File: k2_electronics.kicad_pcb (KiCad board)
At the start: 2 copper layers, 152.1 x 87.5 mm, 62 parts, among them J1 Conn_02x03_Odd_Even, Q1 Q_NMOS_GSD, SW1 SW_SPST, SW10 SW_SPST, SW11 SW_SPST, SW12 SW_SPST, SW13 SW_SPST, SW14 SW_SPST, SW15 SW_SPST, SW16 SW_SPST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

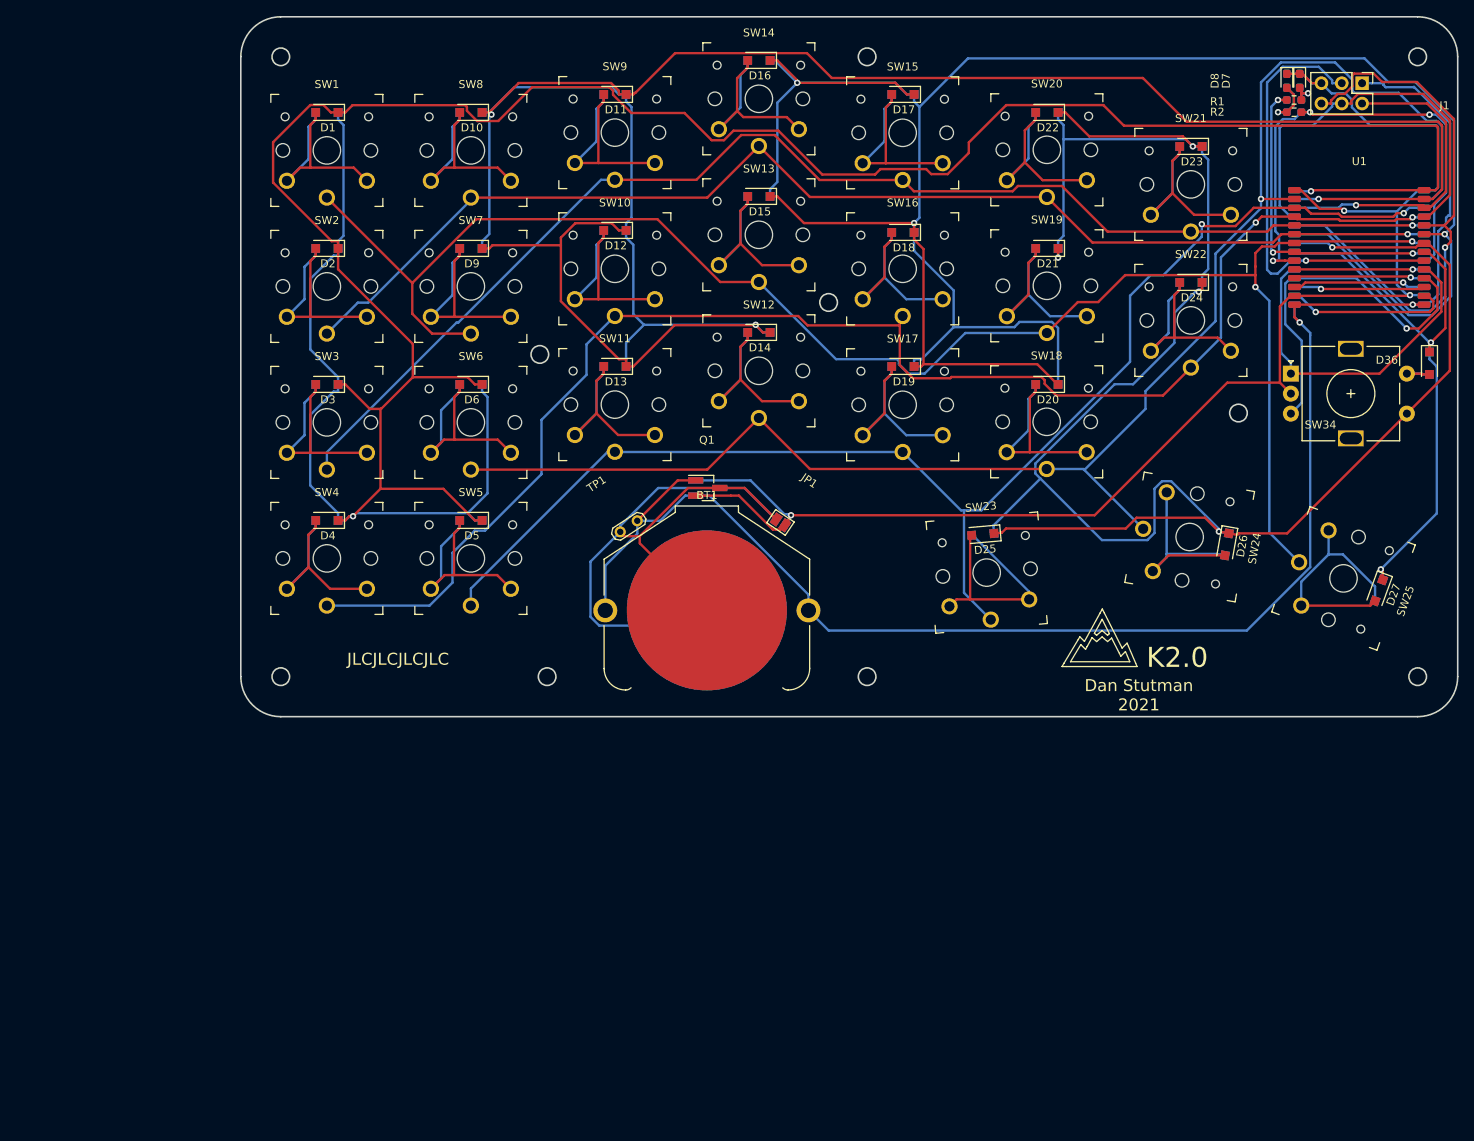
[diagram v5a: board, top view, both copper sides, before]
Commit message: Switch to NPTH holes
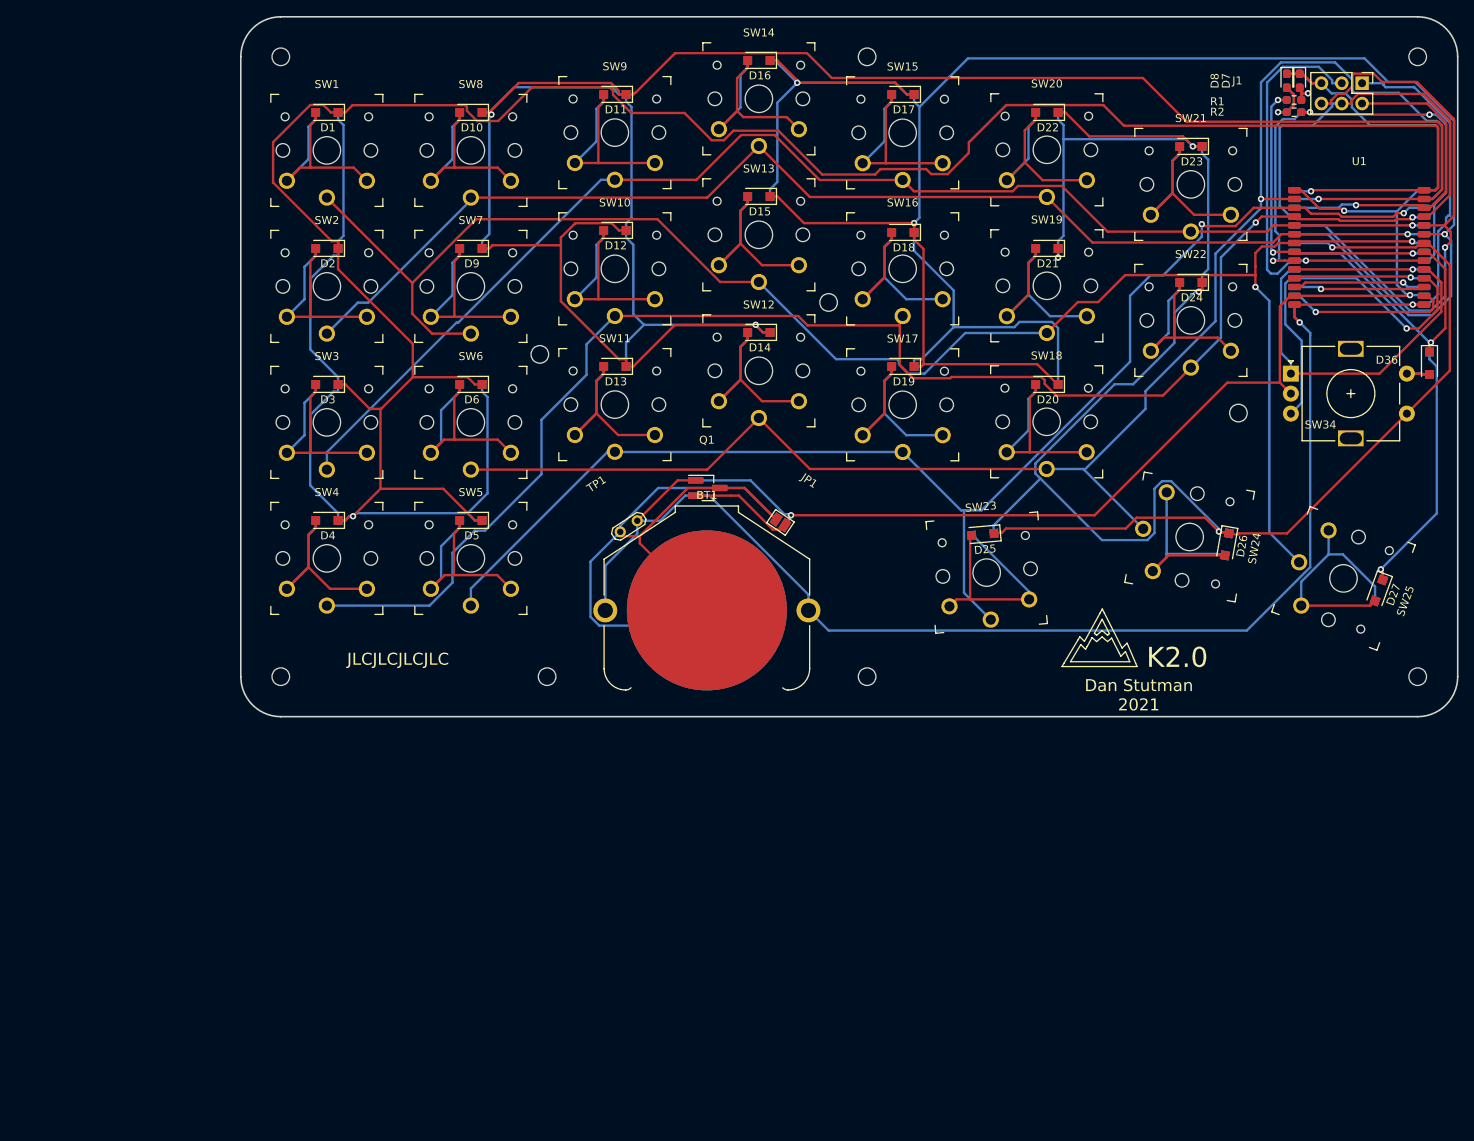
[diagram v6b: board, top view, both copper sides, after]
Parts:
- added REF**: M2 Hole, k2:M2_Hole, F.Cu at (158.5, 132.8)
- added REF**: M2 Hole, k2:M2_Hole, F.Cu at (85.2, 132.8)
- added REF**: M2 Hole, k2:M2_Hole, F.Cu at (158.5, 55.3)
- added REF**: M2 Hole, k2:M2_Hole, F.Cu at (227.4, 55.3)
- added REF**: M2 Hole, k2:M2_Hole, F.Cu at (204.9, 99.8)
- added REF**: M2 Hole, k2:M2_Hole, F.Cu at (227.4, 132.8)
- added REF**: M2 Hole, k2:M2_Hole, F.Cu at (153.7, 86.0)
- added REF**: M2 Hole, k2:M2_Hole, F.Cu at (85.2, 55.3)
- added REF**: M2 Hole, k2:M2_Hole, F.Cu at (117.6, 92.5)
- added REF**: M2 Hole, k2:M2_Hole, F.Cu at (118.5, 132.8)
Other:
- outline, holes or cut-outs redrawn

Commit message: PCB mount
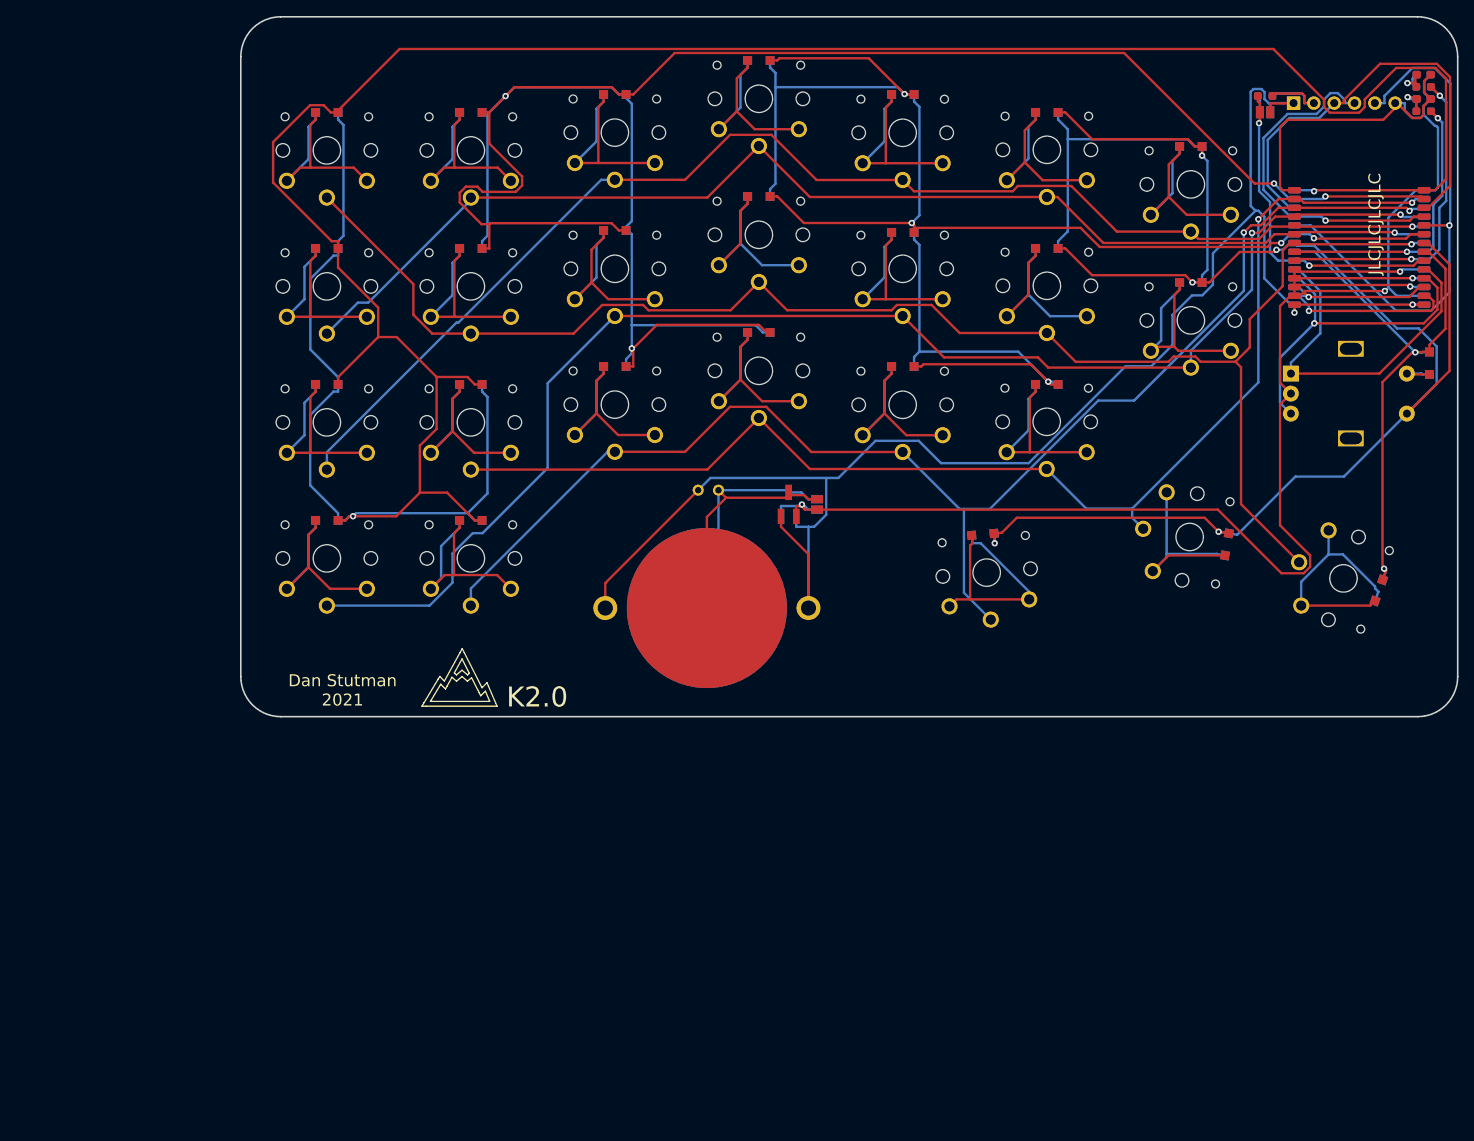
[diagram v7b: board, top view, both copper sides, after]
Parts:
- removed REF** (x10): M2 Hole, k2:M2_Hole
- added JP4: SolderJumper_2_Open, k2:SolderJumper-2_P1.3mm_Open_Pad1.0x1.5mm_reversible, F.Cu at (208.3, 62.2)
- added R3: R_Small_US, k2:R_0603_1608Metric_Pad0.98x0.95mm_HandSolder_reversible, F.Cu at (208.3, 60.2)
- J1: value Conn_02x03_Odd_Even -> Conn_01x06; footprint Connector_PinHeader_2.54mm:PinHeader_2x03_P2.54mm_Vertical -> k2:PinHeader_1x06_P2.54mm_Horizontal
- SW34: footprint Rotary_Encoder:RotaryEncoder_Alps_EC11E-Switch_Vertical_H20mm -> k2:RotaryEncoder_Alps_EC11E-Switch_Vertical_H20mm
- TP1: footprint TestPoint:TestPoint_2Pads_Pitch2.54mm_Drill0.8mm -> k2:TestPoint_2Pads_Pitch2.54mm_Drill0.8mm
- moved D8 17.1 mm to (228.1, 57.5), turned to 180 degrees
- moved R2 16.5 mm to (228.1, 59.1)
- moved R1 16.3 mm to (228.1, 62.1), turned to 0 degrees
- moved D7 15.7 mm to (228.1, 60.6), turned to 180 degrees
- moved Q1 10.3 mm to (148.7, 111.3), turned to 90 degrees
- moved J1 8.92 mm to (211.8, 61.1), turned to 90 degrees
- moved TP1 8.52 mm to (137.4, 109.5), turned to 0 degrees
- moved JP1 5.10 mm to (152.3, 111.3), turned to 270 degrees
- moved BT1 0.29 mm to (138.5, 124.2)
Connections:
- J1 pad 2: /SWCLK -> Net-(J1-Pad2)
- J1 pad 3: /~RESET -> /SWCLK
- J1 pad 5: GND -> /SWO
- J1 pad 6: /SWO -> GND
- U1 pad 10: Net-(U1-Pad10) -> GND
- U1 pad 11: Net-(U1-Pad11) -> GND
- U1 pad 12: Net-(U1-Pad12) -> GND
- U1 pad 16: Net-(U1-Pad16) -> GND
- U1 pad 17: Net-(U1-Pad17) -> GND
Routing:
- net GND: track 194.1 -> 297.8 mm, vias 3 -> 7
- net Net-(D15-Pad1): track 294.7 -> 215.0 mm, vias 3 -> 5
- net Net-(SW12-Pad1): track 192.7 -> 158.0 mm, vias 1 -> 2
- net Net-(BT1-Pad2): track 88.4 -> 56.5 mm
- net Net-(D21-Pad1): track 257.9 -> 229.6 mm
- net Net-(U1-Pad16): track 20.7 -> 0.00 mm, vias 1 -> 0
- net Net-(R2-Pad1): track 62.6 -> 41.9 mm, vias 3 -> 2
- net Net-(SW1-Pad1): track 212.0 -> 194.2 mm, vias 2 -> 1
- net Net-(U1-Pad12): track 16.7 -> 0.00 mm, vias 1 -> 0
- net Net-(D10-Pad1): track 305.3 -> 288.8 mm, vias 3 -> 4
- net Net-(U1-Pad17): track 16.4 -> 0.00 mm, vias 1 -> 0
- net Net-(U1-Pad11): track 16.4 -> 0.00 mm, vias 1 -> 0
- net Net-(U1-Pad10): track 16.2 -> 0.00 mm, vias 1 -> 0
- net /SWCLK: track 40.3 -> 55.8 mm, vias 1 -> 0
- net Net-(J1-Pad2): track 0.00 -> 12.7 mm
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
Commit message: Fix module footprint
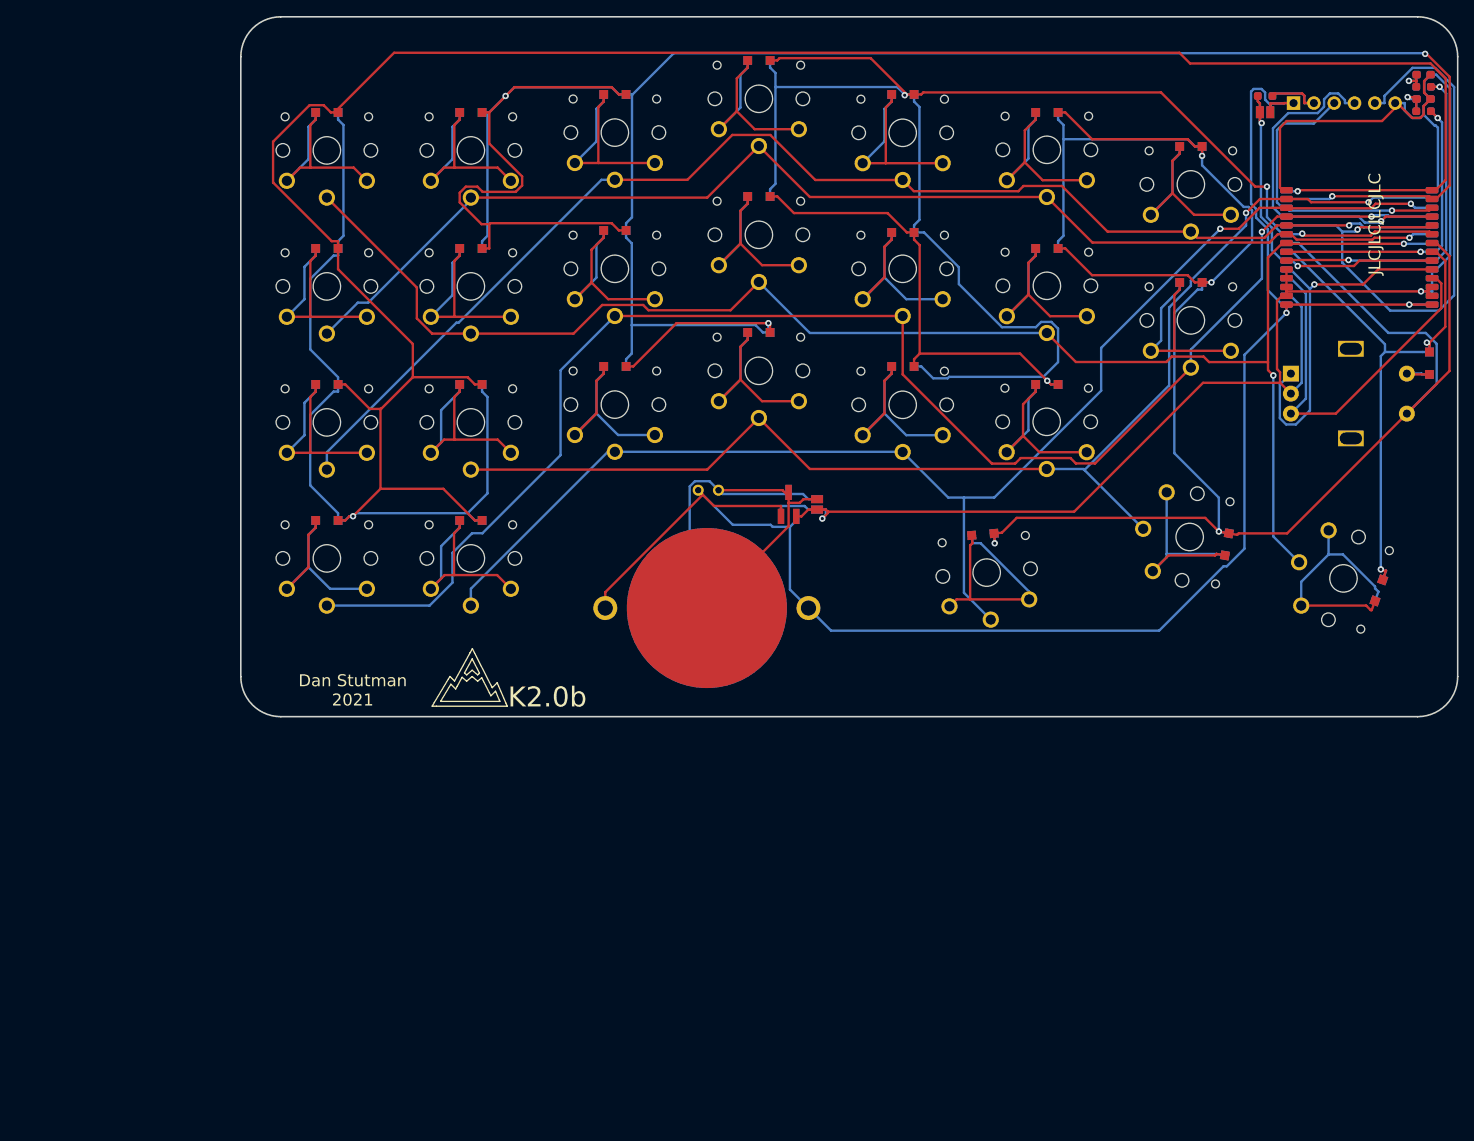
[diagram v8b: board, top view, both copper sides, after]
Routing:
- net GND: track 297.8 -> 217.4 mm, vias 7 -> 2
- net Net-(D15-Pad1): track 215.0 -> 255.2 mm, vias 5 -> 4
- net Net-(D10-Pad1): track 288.8 -> 320.1 mm
- net Net-(D21-Pad1): track 229.6 -> 257.7 mm, vias 5 -> 4
- net /SWCLK: track 55.8 -> 37.5 mm, vias 0 -> 1
- net Net-(SW10-Pad1): track 176.6 -> 191.7 mm
- net /SWO: track 66.6 -> 79.3 mm
- net VDD: track 204.7 -> 213.2 mm
- net Net-(BT1-Pad2): track 56.5 -> 64.9 mm
- net Net-(SW34-PadB): track 41.7 -> 47.8 mm, vias 1 -> 0
- net Net-(D1-Pad1): track 375.9 -> 370.7 mm
- net Net-(SW11-Pad1): track 171.4 -> 167.0 mm
- net Net-(SW1-Pad1): track 194.2 -> 195.9 mm, vias 1 -> 2
- net Net-(SW34-PadA): track 44.7 -> 46.4 mm, vias 0 -> 1
- net Net-(R2-Pad1): track 41.9 -> 43.5 mm
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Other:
- board text added: "K2.0b"
- board text removed: "K2.0"
